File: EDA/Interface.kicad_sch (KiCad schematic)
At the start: 1 part, among them U1 TF03-TD9P

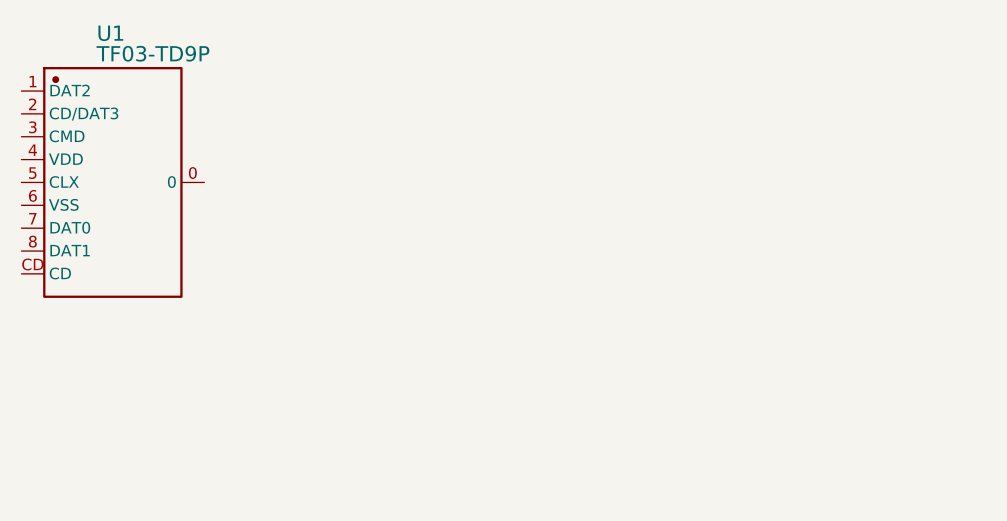
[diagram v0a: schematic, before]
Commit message: Changed STM32 MCU type, and added SDRAM. Micro-SD card slot has also been set up.
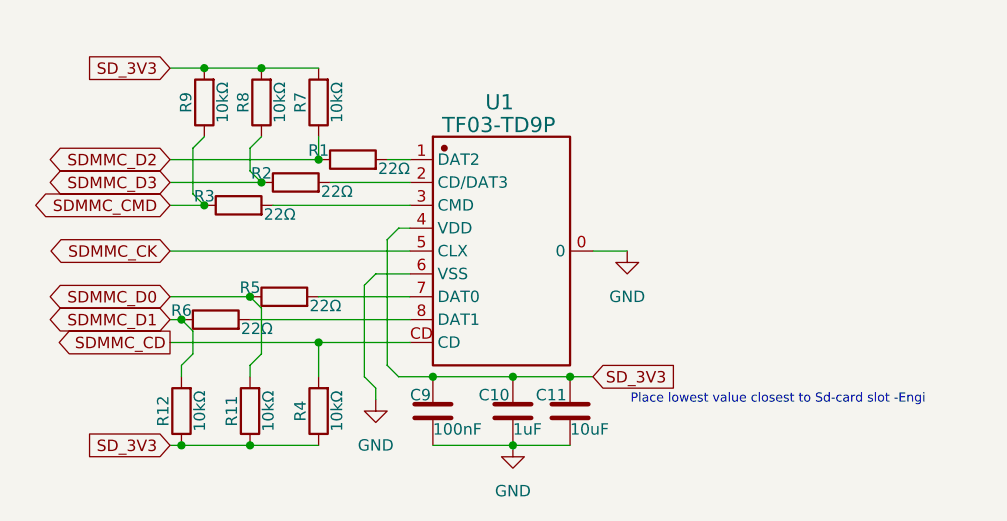
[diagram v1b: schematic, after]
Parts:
- added C10: 1uF, symbol Device:C
- added C11: 10uF, symbol Device:C
- added C9: 100nF, symbol Device:C
- added R1, R2, R3, R5, R6: 22Ω, symbol Device:R
- added R11, R12, R4, R7, R8, R9: 10kΩ, symbol Device:R
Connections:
- net GND: now reaches U1.0
- net GND: now also U1.6 (VSS), C10.2, C11.2, C9.2
- net at U1.1 (DAT2): now also R1.2
- net at U1.2 (CD/DAT3): now also R2.2
- net at U1.3 (CMD): now also R3.2
- net SD_3V3: now reaches U1.4 (VDD)
- net SD_3V3: now also C10.1, C11.1, C9.1, R11.1, R12.1, R4.1, R7.2, R8.2, R9.2
- net SDMMC_CK: now reaches U1.5 (CLX)
- net at U1.7 (DAT0): now also R5.2
- net at U1.8 (DAT1): now also R6.2
- net SDMMC_CD: now reaches U1.CD
- net SDMMC_CD: now also R4.2
- new net SDMMC_CMD: R3.1, R9.1
- new net SDMMC_D0: R11.2, R5.1
- new net SDMMC_D1: R12.2, R6.1
- new net SDMMC_D2: R1.1, R7.1
- new net SDMMC_D3: R2.1, R8.1
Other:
- note added: "Place lowest value closest to Sd-card slot -Engi"
- moved on the sheet: U1

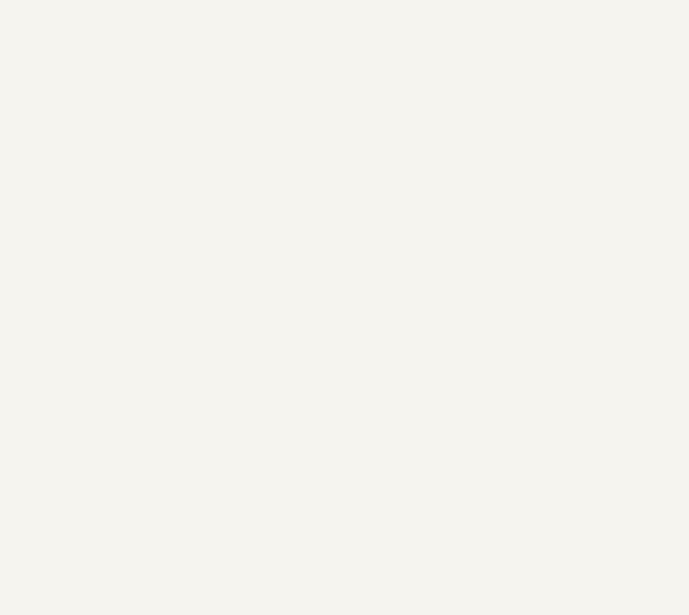
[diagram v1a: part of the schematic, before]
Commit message: added smoothing capacitors to PD IC
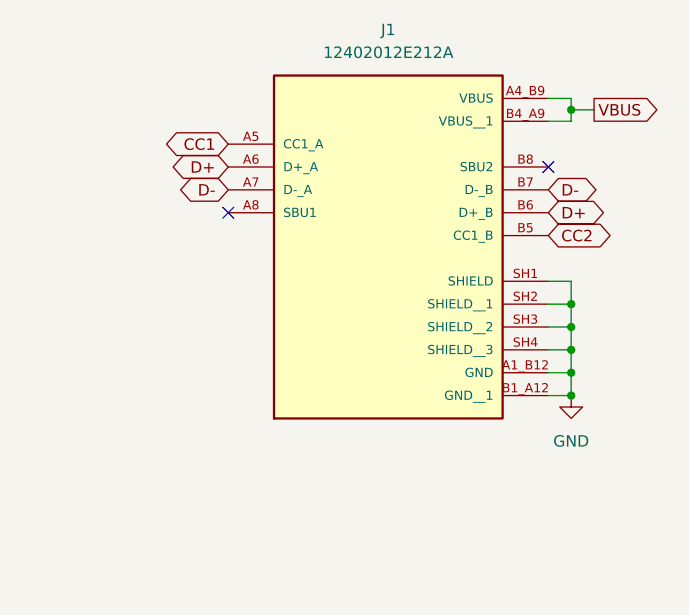
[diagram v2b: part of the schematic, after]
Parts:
- added J1: 12402012E212A, CANSAT-lib:AMPHENOL_USB-C_12402012E212A, symbol CANSAT-lib:12402012E212A
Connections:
- net GND: now also J1.A1_B12 (GND), J1.B1_A12 (GND__1), J1.SH1 (SHIELD), J1.SH2 (SHIELD__1), J1.SH3 (SHIELD__2), J1.SH4 (SHIELD__3)
- new net CC1: J1.A5 (CC1_A)
- new net CC2: J1.B5 (CC1_B)
- new net D+: J1.A6 (D+_A), J1.B6 (D+_B)
- new net D-: J1.A7 (D-_A), J1.B7 (D-_B)
- new net VBUS: J1.A4_B9 (VBUS), J1.B4_A9 (VBUS__1)
- no-connect marks 0 -> 2

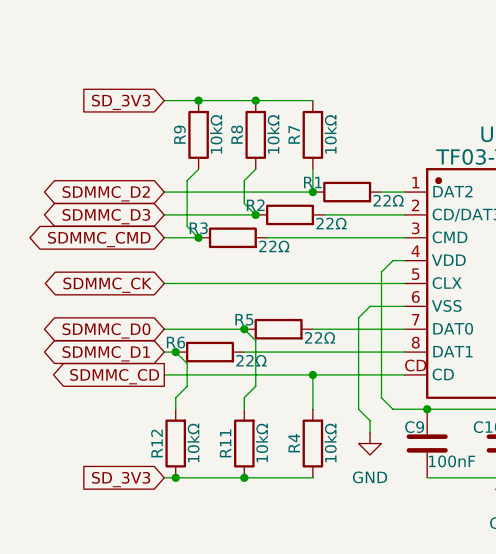
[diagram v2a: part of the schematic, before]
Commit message: Did some scheamtic restruscturing as well as hooked up SDRAM and Micro-SD to STM32 core. Additional low power STM32 has also been added to power control. Firmware .IOC files have also been added for both STM32's
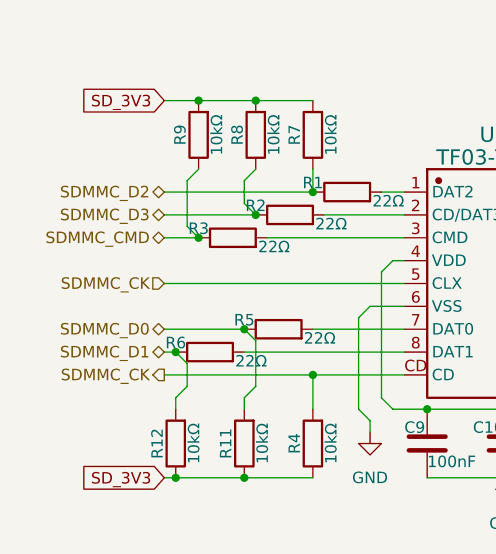
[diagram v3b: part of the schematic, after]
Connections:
- net SDMMC_CD is gone; now on net SDMMC_CK: R4.2, U1.CD
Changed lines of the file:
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@@
-		)
-	)
-	(global_label "SDMMC_D1"
-		(shape bidirectional)
-		(at 55.88 109.22 180)
-		(fields_autoplaced yes)
-		(effects
-			(font
-				(size 1.27 1.27)
-			)
-			(justify right)
-		)
-		(property "Intersheetrefs" "${INTERSHEET_REFS}"
-			(at 41.6841 109.22 0)
-			(effects
-				(font
-					(size 1.27 1.27)
-				)
-				(justify right)
-				(hide yes)
-			)
-		)
-	)
-	(global_label "SDMMC_CD"
-		(shape output)
-		(at 55.88 111.76 180)
-		(fields_autoplaced yes)
-		(effects
-			(font
-				(size 1.27 1.27)
-			)
-			(justify right)
-		)
-		(property "Intersheetrefs" "${INTERSHEET_REFS}"
-			(at 42.7349 111.76 0)
-			(effects
-				(font
-					(size 1.27 1.27)
-				)
-				(justify right)
-				(hide yes)
-			)
 		)
 	)
@@
 		)
 	)
-	(global_label "SDMMC_CMD"
-		(shape bidirectional)
-		(at 55.88 96.52 180)
-		(fields_autoplaced yes)
-		(effects
-			(font
-				(size 1.27 1.27)
-			)
-			(justify right)
-		)
-		(property "Intersheetrefs" "${INTERSHEET_REFS}"
-			(at 40.1722 96.52 0)
-			(effects
-				(font
-					(size 1.27 1.27)
-				)
-				(justify right)
-				(hide yes)
-			)
-		)
-	)
 	(global_label "VBUS"
 		(shape output)
@@
 		)
 	)
-	(global_label "SDMMC_D2"
-		(shape bidirectional)
-		(at 55.88 91.44 180)
-		(fields_autoplaced yes)
-		(effects
-			(font
-				(size 1.27 1.27)
-			)
-			(justify right)
-		)
-		(property "Intersheetrefs" "${INTERSHEET_REFS}"
-			(at 41.6841 91.44 0)
-			(effects
-				(font
-					(size 1.27 1.27)
-				)
-				(justify right)
-				(hide yes)
-			)
-		)
-	)
-	(global_label "SDMMC_D3"
-		(shape bidirectional)
-		(at 55.88 93.98 180)
-		(fields_autoplaced yes)
-		(effects
-			(font
-				(size 1.27 1.27)
-			)
-			(justify right)
-		)
-		(property "Intersheetrefs" "${INTERSHEET_REFS}"
-			(at 41.6841 93.98 0)
-			(effects
-				(font
-					(size 1.27 1.27)
-				)
-				(justify right)
-				(hide yes)
-			)
-		)
-	)
 	(global_label "CC2"
 		(shape bidirectional)
@@
 		)
 	)
-	(global_label "SDMMC_CK"
-		(shape bidirectional)
-		(at 55.88 101.6 180)
-		(fields_autoplaced yes)
-		(effects
-			(font
-				(size 1.27 1.27)
-			)
-			(justify right)
-		)
-		(property "Intersheetrefs" "${INTERSHEET_REFS}"
-			(at 41.6236 101.6 0)
-			(effects
-				(font
-					(size 1.27 1.27)
-				)
-				(justify right)
-				(hide yes)
-			)
-		)
-	)
-	(global_label "SDMMC_D0"
-		(shape bidirectional)
-		(at 55.88 106.68 180)
-		(fields_autoplaced yes)
-		(effects
-			(font
-				(size 1.27 1.27)
-			)
-			(justify right)
-		)
-		(property "Intersheetrefs" "${INTERSHEET_REFS}"
-			(at 41.6841 106.68 0)
-			(effects
-				(font
-					(size 1.27 1.27)
-				)
-				(justify right)
-				(hide yes)
-			)
-		)
-	)
 	(global_label "D+"
 		(shape bidirectional)
@@
 		)
 	)
+	(hierarchical_label "SDMMC_CMD"
+		(shape bidirectional)
+		(at 55.88 96.52 180)
+		(effects
+			(font
+				(size 1.27 1.27)
+			)
+			(justify right)
+		)
+	)
+	(hierarchical_label "SDMMC_D1"
+		(shape bidirectional)
+		(at 55.88 109.22 180)
+		(effects
+			(font
+				(size 1.27 1.27)
+			)
+			(justify right)
+		)
+	)
+	(hierarchical_label "SDMMC_D0"
+		(shape bidirectional)
+		(at 55.88 106.68 180)
+		(effects
+			(font
+				(size 1.27 1.27)
+			)
+			(justify right)
+		)
+	)
+	(hierarchical_label "SDMMC_CK"
+		(shape input)
+		(at 55.88 101.6 180)
+		(effects
+			(font
+				(size 1.27 1.27)
+			)
+			(justify right)
+		)
+	)
+	(hierarchical_label "SDMMC_D3"
+		(shape bidirectional)
+		(at 55.88 93.98 180)
+		(effects
+			(font
+				(size 1.27 1.27)
+			)
+			(justify right)
+		)
+	)
+	(hierarchical_label "SDMMC_D2"
+		(shape bidirectional)
+		(at 55.88 91.44 180)
+		(effects
+			(font
+				(size 1.27 1.27)
+			)
+			(justify right)
+		)
+	)
+	(hierarchical_label "SDMMC_CK"
+		(shape output)
+		(at 55.88 111.76 180)
+		(effects
+			(font
+				(size 1.27 1.27)
+			)
+			(justify right)
+		)
+	)
 	(symbol
 		(lib_id "Device:R")
@@
 		)
 		(property "Size" "R0402"
+			(at 66.04 85.09 90)
+			(effects
+				(font
+					(size 1.27 1.27)
+				)
+				(hide yes)
+			)
+		)
+		(property "Type" ""
 			(at 66.04 85.09 90)
 			(effects
@@
 			)
 		)
+		(property "Type" ""
+			(at 100.33 119.38 0)
+			(effects
+				(font
+					(size 1.27 1.27)
+				)
+				(hide yes)
+			)
+		)
 		(pin "1"
 		)
@@
 			)
 		)
+		(property "Type" ""
+			(at 60.96 109.22 90)
+			(effects
+				(font
+					(size 1.27 1.27)
+				)
+				(hide yes)
+			)
+		)
 		(pin "1"
 		)
@@
 			)
 		)
+		(property "Type" ""
+			(at 63.5 96.52 90)
+			(effects
+				(font
+					(size 1.27 1.27)
+				)
+				(hide yes)
+			)
+		)
 		(pin "1"
 		)
@@
 			)
 		)
+		(property "Type" ""
+			(at 64.77 119.38 90)
+			(effects
+				(font
+					(size 1.27 1.27)
+				)
+				(hide yes)
+			)
+		)
 		(pin "1"
 		)
@@
 			)
 		)
+		(property "Type" ""
+			(at 93.98 119.38 0)
+			(effects
+				(font
+					(size 1.27 1.27)
+				)
+				(hide yes)
+			)
+		)
 		(pin "1"
 		)
@@
 			)
 		)
+		(property "Type" ""
+			(at 72.39 119.38 90)
+			(effects
+				(font
+					(size 1.27 1.27)
+				)
+				(hide yes)
+			)
+		)
 		(pin "1"
 		)
@@
 			)
 		)
+		(property "Type" ""
+			(at 171.45 45.72 0)
+			(effects
+				(font
+					(size 1.27 1.27)
+				)
+				(hide yes)
+			)
+		)
 		(pin "A8"
 		)
@@
 			)
 		)
+		(property "Type" ""
+			(at 76.2 91.44 90)
+			(effects
+				(font
+					(size 1.27 1.27)
+				)
+				(hide yes)
+			)
+		)
 		(pin "1"
 		)
@@
 			)
 		)
+		(property "Type" ""
+			(at 69.85 93.98 90)
+			(effects
+				(font
+					(size 1.27 1.27)
+				)
+				(hide yes)
+			)
+		)
 		(pin "1"
 		)
@@
 			)
 		)
+		(property "Type" ""
+			(at 85.09 119.38 0)
+			(effects
+				(font
+					(size 1.27 1.27)
+				)
+				(hide yes)
+			)
+		)
 		(pin "1"
 		)
@@
 			)
 		)
+		(property "Type" ""
+			(at 92.71 101.6 0)
+			(effects
+				(font
+					(size 1.27 1.27)
+				)
+				(hide yes)
+			)
+		)
 		(pin "6"
 		)
@@
 			)
 		)
+		(property "Type" ""
+			(at 57.15 119.38 90)
+			(effects
+				(font
+					(size 1.27 1.27)
+				)
+				(hide yes)
+			)
+		)
 		(pin "1"
 		)
@@
 			)
 		)
+		(property "Type" ""
+			(at 72.39 85.09 90)
+			(effects
+				(font
+					(size 1.27 1.27)
+				)
+				(hide yes)
+			)
+		)
 		(pin "1"
 		)
@@
 			)
 		)
+		(property "Type" ""
+			(at 59.69 85.09 90)
+			(effects
+				(font
+					(size 1.27 1.27)
+				)
+				(hide yes)
+			)
+		)
 		(pin "1"
 		)
@@
 			(at 68.58 106.68 90)
 			(effects
+				(font
+					(size 1.27 1.27)
+				)
+				(hide yes)
+			)
+		)
+		(property "Type" ""
+			(at 68.58 106.68 90)
+			(effects
